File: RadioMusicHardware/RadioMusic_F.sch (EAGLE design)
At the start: 30 parts, among them X1 VERT_SD_CARD

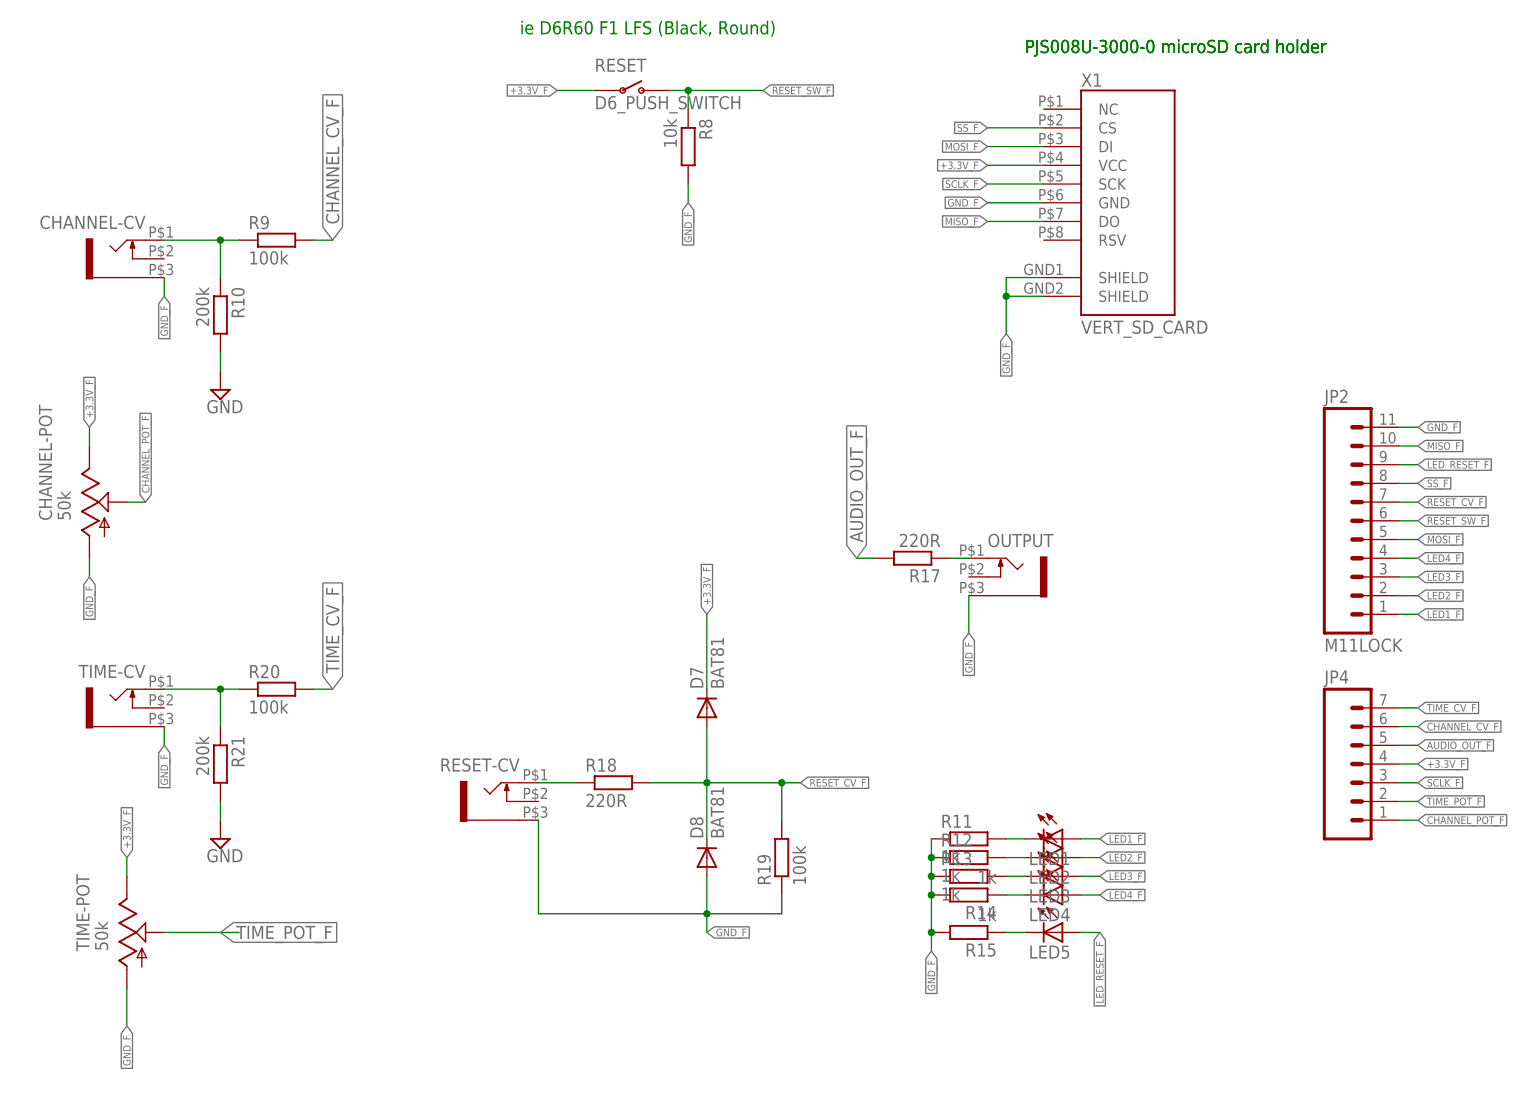
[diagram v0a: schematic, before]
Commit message: Front board reworking
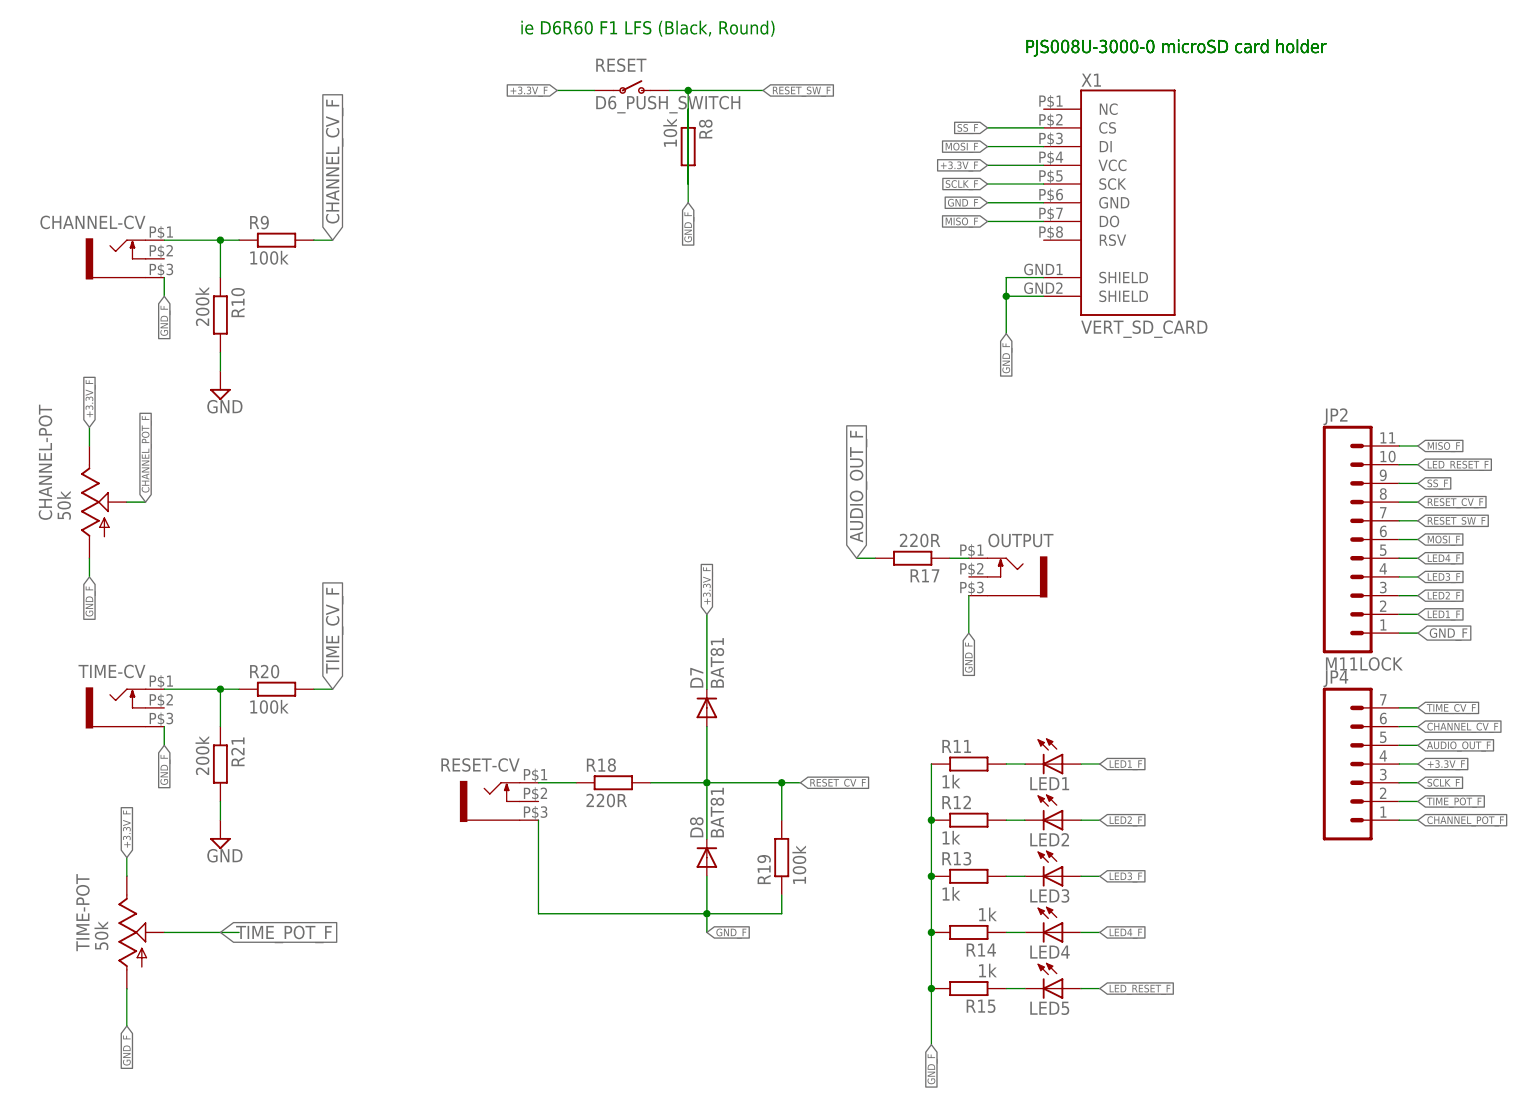
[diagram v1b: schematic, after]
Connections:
- net GND_F: now also JP2.1, R8.1; no longer JP2.11, R8.2
- net LED1_F: now also JP2.2; no longer JP2.1
- net LED2_F: now also JP2.3; no longer JP2.2
- net LED3_F: now also JP2.4; no longer JP2.3
- net LED4_F: now also JP2.5; no longer JP2.4
- net LED_RESET_F: now also JP2.10; no longer JP2.9
- net MISO_F: now also JP2.11; no longer JP2.10
- net MOSI_F: now also JP2.6; no longer JP2.5
- net RESET_CV_F: now also JP2.8; no longer JP2.7
- net RESET_SW_F: now also JP2.7, R8.2; no longer JP2.6, R8.1
- net SS_F: now also JP2.9; no longer JP2.8
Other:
- moved on the sheet: JP2, LED1, LED2, LED4, LED5, R11, R12, R14, R15
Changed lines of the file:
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@@
 <instance part="RESET" gate="G$1" x="99.06" y="137.16"/>
 <instance part="R8" gate="G$1" x="106.68" y="129.54" rot="R270"/>
-<instance part="LED1" gate="G$1" x="157.48" y="35.56" rot="R270"/>
-<instance part="LED2" gate="G$1" x="157.48" y="33.02" rot="R270"/>
+<instance part="LED1" gate="G$1" x="157.48" y="45.72" rot="R270"/>
+<instance part="LED2" gate="G$1" x="157.48" y="38.1" rot="R270"/>
 <instance part="LED3" gate="G$1" x="157.48" y="30.48" rot="R270"/>
-<instance part="LED4" gate="G$1" x="157.48" y="27.94" rot="R270"/>
-<instance part="R11" gate="G$1" x="144.78" y="35.56"/>
-<instance part="R12" gate="G$1" x="144.78" y="33.02"/>
+<instance part="LED4" gate="G$1" x="157.48" y="22.86" rot="R270"/>
+<instance part="R11" gate="G$1" x="144.78" y="45.72"/>
+<instance part="R12" gate="G$1" x="144.78" y="38.1"/>
 <instance part="R13" gate="G$1" x="144.78" y="30.48"/>
-<instance part="R14" gate="G$1" x="144.78" y="27.94" rot="R180"/>
+<instance part="R14" gate="G$1" x="144.78" y="22.86" rot="R180"/>
 <instance part="X1" gate="G$1" x="162.56" y="121.92"/>
-<instance part="LED5" gate="G$1" x="157.48" y="22.86" rot="R270"/>
-<instance part="R15" gate="G$1" x="144.78" y="22.86" rot="R180"/>
-<instance part="JP2" gate="G$1" x="193.04" y="78.74"/>
+<instance part="LED5" gate="G$1" x="157.48" y="15.24" rot="R270"/>
+<instance part="R15" gate="G$1" x="144.78" y="15.24" rot="R180"/>
+<instance part="JP2" gate="G$1" x="193.04" y="76.2"/>
 <instance part="JP4" gate="G$1" x="198.12" y="43.18"/>
 </instances>
@@
 <pinref part="LED1" gate="G$1" pin="C"/>
 <pinref part="R11" gate="G$1" pin="2"/>
-<wire x1="152.4" y1="35.56" x2="149.86" y2="35.56" width="0.1524" layer="91"/>
+<wire x1="152.4" y1="45.72" x2="149.86" y2="45.72" width="0.1524" layer="91"/>
 </segment>
 </net>
@@
 <pinref part="LED2" gate="G$1" pin="C"/>
 <pinref part="R12" gate="G$1" pin="2"/>
-<wire x1="149.86" y1="33.02" x2="152.4" y2="33.02" width="0.1524" layer="91"/>
+<wire x1="149.86" y1="38.1" x2="152.4" y2="38.1" width="0.1524" layer="91"/>
 </segment>
 </net>
@@
 <pinref part="LED4" gate="G$1" pin="C"/>
 <pinref part="R14" gate="G$1" pin="1"/>
-<wire x1="149.86" y1="27.94" x2="152.4" y2="27.94" width="0.1524" layer="91"/>
+<wire x1="149.86" y1="22.86" x2="152.4" y2="22.86" width="0.1524" layer="91"/>
 </segment>
 </net>
@@
 </segment>
 <segment>
-<pinref part="JP2" gate="G$1" pin="10"/>
+<pinref part="JP2" gate="G$1" pin="11"/>
 <wire x1="205.74" y1="88.9" x2="203.2" y2="88.9" width="0.1524" layer="91"/>
 <label x="205.74" y="88.9" size="1.016" layer="95" xref="yes"/>
@@
 <pinref part="LED5" gate="G$1" pin="C"/>
 <pinref part="R15" gate="G$1" pin="1"/>
-<wire x1="149.86" y1="22.86" x2="152.4" y2="22.86" width="0.1524" layer="91"/>
+<wire x1="149.86" y1="15.24" x2="152.4" y2="15.24" width="0.1524" layer="91"/>
 </segment>
 </net>
@@
 <net name="RESET_SW_F" class="0">
 <segment>
-<pinref part="JP2" gate="G$1" pin="6"/>
+<pinref part="JP2" gate="G$1" pin="7"/>
 <wire x1="205.74" y1="78.74" x2="203.2" y2="78.74" width="0.1524" layer="91"/>
 <label x="205.74" y="78.74" size="1.016" layer="95" xref="yes"/>
@@
 <pinref part="RESET" gate="G$1" pin="O"/>
 <wire x1="104.14" y1="137.16" x2="106.68" y2="137.16" width="0.1524" layer="91"/>
-<pinref part="R8" gate="G$1" pin="1"/>
+<pinref part="R8" gate="G$1" pin="2"/>
 <wire x1="106.68" y1="137.16" x2="116.84" y2="137.16" width="0.1524" layer="91"/>
-<wire x1="106.68" y1="134.62" x2="106.68" y2="137.16" width="0.1524" layer="91"/>
+<wire x1="106.68" y1="124.46" x2="106.68" y2="137.16" width="0.1524" layer="91"/>
 <junction x="106.68" y="137.16"/>
 <label x="116.84" y="137.16" size="1.016" layer="95" xref="yes"/>
@@
 <segment>
 <pinref part="LED5" gate="G$1" pin="A"/>
-<wire x1="162.56" y1="22.86" x2="160.02" y2="22.86" width="0.1524" layer="91"/>
-<label x="162.56" y="22.86" size="1.016" layer="95" rot="R270" xref="yes"/>
-</segment>
-<segment>
-<pinref part="JP2" gate="G$1" pin="9"/>
+<wire x1="162.56" y1="15.24" x2="160.02" y2="15.24" width="0.1524" layer="91"/>
+<label x="162.56" y="15.24" size="1.016" layer="95" xref="yes"/>
+</segment>
+<segment>
+<pinref part="JP2" gate="G$1" pin="10"/>
 <wire x1="205.74" y1="86.36" x2="203.2" y2="86.36" width="0.1524" layer="91"/>
 <label x="205.74" y="86.36" size="1.016" layer="95" xref="yes"/>
@@
 <net name="LED4_F" class="0">
 <segment>
-<pinref part="JP2" gate="G$1" pin="4"/>
+<pinref part="JP2" gate="G$1" pin="5"/>
 <wire x1="205.74" y1="73.66" x2="203.2" y2="73.66" width="0.1524" layer="91"/>
 <label x="205.74" y="73.66" size="1.016" layer="95" xref="yes"/>
@@
 <segment>
 <pinref part="LED4" gate="G$1" pin="A"/>
-<wire x1="162.56" y1="27.94" x2="160.02" y2="27.94" width="0.1524" layer="91"/>
-<label x="162.56" y="27.94" size="1.016" layer="95" xref="yes"/>
+<wire x1="162.56" y1="22.86" x2="160.02" y2="22.86" width="0.1524" layer="91"/>
+<label x="162.56" y="22.86" size="1.016" layer="95" xref="yes"/>
 </segment>
 </net>
 <net name="LED3_F" class="0">
 <segment>
-<pinref part="JP2" gate="G$1" pin="3"/>
+<pinref part="JP2" gate="G$1" pin="4"/>
 <wire x1="205.74" y1="71.12" x2="203.2" y2="71.12" width="0.1524" layer="91"/>
 <label x="205.74" y="71.12" size="1.016" layer="95" xref="yes"/>
@@
 <net name="LED2_F" class="0">
 <segment>
-<pinref part="JP2" gate="G$1" pin="2"/>
+<pinref part="JP2" gate="G$1" pin="3"/>
 <wire x1="205.74" y1="68.58" x2="203.2" y2="68.58" width="0.1524" layer="91"/>
 <label x="205.74" y="68.58" size="1.016" layer="95" xref="yes"/>
@@
 <segment>
 <pinref part="LED2" gate="G$1" pin="A"/>
-<wire x1="162.56" y1="33.02" x2="160.02" y2="33.02" width="0.1524" layer="91"/>
-<label x="162.56" y="33.02" size="1.016" layer="95" xref="yes"/>
+<wire x1="162.56" y1="38.1" x2="160.02" y2="38.1" width="0.1524" layer="91"/>
+<label x="162.56" y="38.1" size="1.016" layer="95" xref="yes"/>
 </segment>
 </net>
 <net name="LED1_F" class="0">
 <segment>
-<pinref part="JP2" gate="G$1" pin="1"/>
+<pinref part="JP2" gate="G$1" pin="2"/>
 <wire x1="205.74" y1="66.04" x2="203.2" y2="66.04" width="0.1524" layer="91"/>
 <label x="205.74" y="66.04" size="1.016" layer="95" xref="yes"/>
@@
 <segment>
 <pinref part="LED1" gate="G$1" pin="A"/>
-<wire x1="162.56" y1="35.56" x2="160.02" y2="35.56" width="0.1524" layer="91"/>
-<label x="162.56" y="35.56" size="1.016" layer="95" xref="yes"/>
+<wire x1="162.56" y1="45.72" x2="160.02" y2="45.72" width="0.1524" layer="91"/>
+<label x="162.56" y="45.72" size="1.016" layer="95" xref="yes"/>
 </segment>
 </net>
@@
 </net>
 <net name="GND_F" class="0">
-<segment>
-<pinref part="JP2" gate="G$1" pin="11"/>
-<wire x1="205.74" y1="91.44" x2="203.2" y2="91.44" width="0.1524" layer="91"/>
-<label x="205.74" y="91.44" size="1.016" layer="95" xref="yes"/>
-</segment>
 <segment>
 <pinref part="X1" gate="G$1" pin="GND"/>
@@
 </segment>
 <segment>
-<wire x1="139.7" y1="35.56" x2="139.7" y2="33.02" width="0.1524" layer="91"/>
+<wire x1="139.7" y1="45.72" x2="139.7" y2="38.1" width="0.1524" layer="91"/>
 <pinref part="R11" gate="G$1" pin="1"/>
 <pinref part="R12" gate="G$1" pin="1"/>
-<wire x1="139.7" y1="33.02" x2="139.7" y2="30.48" width="0.1524" layer="91"/>
-<junction x="139.7" y="33.02"/>
+<wire x1="139.7" y1="38.1" x2="139.7" y2="30.48" width="0.1524" layer="91"/>
+<junction x="139.7" y="38.1"/>
 <pinref part="R13" gate="G$1" pin="1"/>
-<wire x1="139.7" y1="30.48" x2="139.7" y2="27.94" width="0.1524" layer="91"/>
+<wire x1="139.7" y1="30.48" x2="139.7" y2="22.86" width="0.1524" layer="91"/>
 <junction x="139.7" y="30.48"/>
 <pinref part="R14" gate="G$1" pin="2"/>
-<wire x1="139.7" y1="27.94" x2="139.7" y2="22.86" width="0.1524" layer="91"/>
-<junction x="139.7" y="27.94"/>
+<wire x1="139.7" y1="22.86" x2="139.7" y2="15.24" width="0.1524" layer="91"/>
+<junction x="139.7" y="22.86"/>
 <pinref part="R15" gate="G$1" pin="2"/>
-<wire x1="139.7" y1="22.86" x2="139.7" y2="20.32" width="0.1524" layer="91"/>
-<junction x="139.7" y="22.86"/>
-<label x="139.7" y="20.32" size="1.016" layer="95" rot="R270" xref="yes"/>
+<wire x1="139.7" y1="15.24" x2="139.7" y2="7.62" width="0.1524" layer="91"/>
+<junction x="139.7" y="15.24"/>
+<label x="139.7" y="7.62" size="1.016" layer="95" rot="R270" xref="yes"/>
 </segment>
 <segment>
@@
 </segment>
 <segment>
-<pinref part="R8" gate="G$1" pin="2"/>
-<wire x1="106.68" y1="121.92" x2="106.68" y2="124.46" width="0.1524" layer="91"/>
+<pinref part="R8" gate="G$1" pin="1"/>
+<wire x1="106.68" y1="121.92" x2="106.68" y2="134.62" width="0.1524" layer="91"/>
 <label x="106.68" y="121.92" size="1.016" layer="95" rot="R270" xref="yes"/>
+</segment>
+<segment>
+<pinref part="JP2" gate="G$1" pin="1"/>
+<wire x1="205.74" y1="63.5" x2="203.2" y2="63.5" width="0.1524" layer="91"/>
+<label x="205.74" y="63.5" size="1.27" layer="95" xref="yes"/>
 </segment>
 </net>
@@
 </segment>
 <segment>
-<pinref part="JP2" gate="G$1" pin="7"/>
+<pinref part="JP2" gate="G$1" pin="8"/>
 <wire x1="205.74" y1="81.28" x2="203.2" y2="81.28" width="0.1524" layer="91"/>
 <label x="205.74" y="81.28" size="1.016" layer="95" xref="yes"/>
@@
 </segment>
 <segment>
-<pinref part="JP2" gate="G$1" pin="5"/>
+<pinref part="JP2" gate="G$1" pin="6"/>
 <wire x1="205.74" y1="76.2" x2="203.2" y2="76.2" width="0.1524" layer="91"/>
 <label x="205.74" y="76.2" size="1.016" layer="95" xref="yes"/>
@@
 </segment>
 <segment>
-<pinref part="JP2" gate="G$1" pin="8"/>
+<pinref part="JP2" gate="G$1" pin="9"/>
 <wire x1="205.74" y1="83.82" x2="203.2" y2="83.82" width="0.1524" layer="91"/>
 <label x="205.74" y="83.82" size="1.016" layer="95" xref="yes"/>
